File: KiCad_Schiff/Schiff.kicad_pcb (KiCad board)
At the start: 2 copper layers, 150 x 60 mm, 40 parts, among them J1 Conn_01x02, J2 L298N, J3 AMS1117-Module, J4 L298N, J5 Screw_Terminal_01x02, J6 Screw_Terminal_01x02, M1 Motor_Servo, M2 Motor_Servo, M3 Motor_Servo, SW1 SW_Wuerth_450301014042, SW2 SW_Wuerth_450301014042, U1 NRF24L01_Breakout

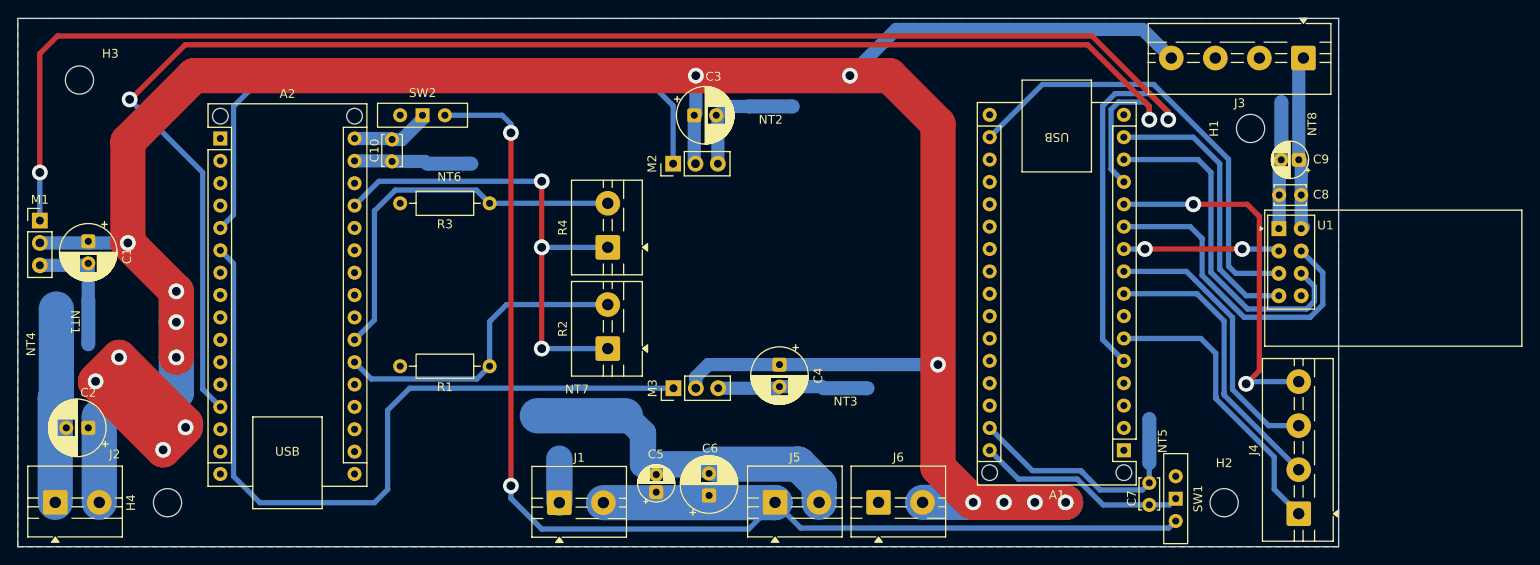
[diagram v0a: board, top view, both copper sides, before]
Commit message: Added plane on front
Added plane on front and put it on ground, to reduce machining
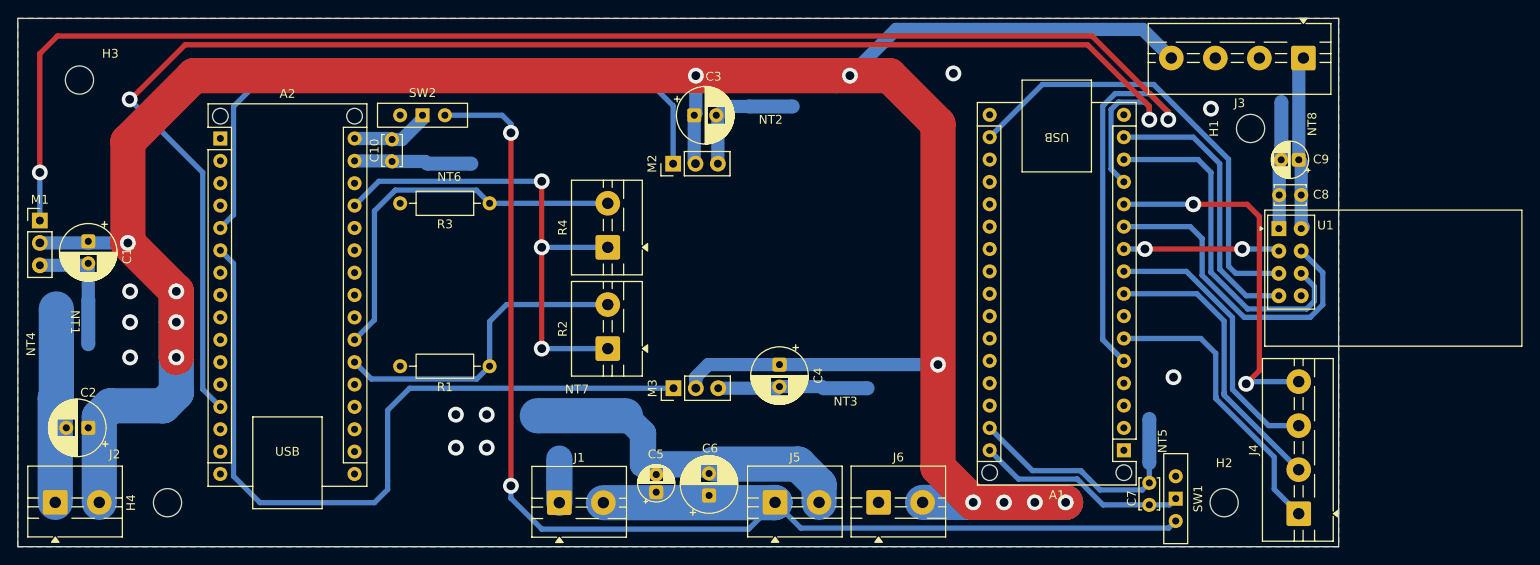
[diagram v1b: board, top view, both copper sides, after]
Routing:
- net /GND_PLANE: track 34.1 -> 5.00 mm, vias 4 -> 10
- added copper zone on F.Cu, net /GND_PLANE
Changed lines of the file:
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@@
 		(net 66)
 	)
-	(segment
-		(start 39 66)
-		(end 31.5 58.5)
-		(width 4)
-		(layer "F.Cu")
-		(net 67)
-	)
-	(segment
-		(start 39.05188 66.044315)
-		(end 39.007565 66)
-		(width 4)
-		(layer "F.Cu")
-		(net 67)
-	)
-	(segment
-		(start 39.007565 66)
-		(end 39 66)
-		(width 4)
-		(layer "F.Cu")
-		(net 67)
-	)
-	(segment
-		(start 28.827888 61.327888)
-		(end 28.827888 61.213147)
-		(width 4)
-		(layer "F.Cu")
-		(net 67)
-	)
-	(segment
-		(start 29 61.041035)
-		(end 29 61)
-		(width 4)
-		(layer "F.Cu")
-		(net 67)
-	)
-	(segment
-		(start 36.5 69)
-		(end 28.827888 61.327888)
-		(width 4)
-		(layer "F.Cu")
-		(net 67)
-	)
-	(segment
-		(start 39.05188 66.44812)
-		(end 36.5 69)
-		(width 4)
-		(layer "F.Cu")
-		(net 67)
-	)
-	(segment
-		(start 28.827888 61.213147)
-		(end 29 61.041035)
-		(width 4)
-		(layer "F.Cu")
-		(net 67)
-	)
-	(segment
-		(start 29 61)
-		(end 31.5 58.5)
-		(width 4)
-		(layer "F.Cu")
-		(net 67)
-	)
-	(via
-		(at 36.5 69)
-		(size 1.8)
-		(drill 1)
-		(layers "F.Cu" "B.Cu")
-		(free yes)
-		(net 67)
-	)
-	(via
-		(at 39.05188 66.44812)
-		(size 1.8)
-		(drill 1)
-		(layers "F.Cu" "B.Cu")
-		(free yes)
-		(net 67)
-	)
-	(via
-		(at 31.5 58.5)
-		(size 1.8)
-		(drill 1)
-		(layers "F.Cu" "B.Cu")
-		(free yes)
-		(net 67)
-	)
-	(via
-		(at 28.827888 61.213147)
+	(via
+		(at 73.25 68.75)
+		(size 1.8)
+		(drill 1)
+		(layers "F.Cu" "B.Cu")
+		(free yes)
+		(net 67)
+	)
+	(via
+		(at 69.75 65)
+		(size 1.8)
+		(drill 1)
+		(layers "F.Cu" "B.Cu")
+		(free yes)
+		(net 67)
+	)
+	(via
+		(at 32.75 51)
+		(size 1.8)
+		(drill 1)
+		(layers "F.Cu" "B.Cu")
+		(free yes)
+		(net 67)
+	)
+	(via
+		(at 151.25 60.75)
+		(size 1.8)
+		(drill 1)
+		(layers "F.Cu" "B.Cu")
+		(free yes)
+		(net 67)
+	)
+	(via
+		(at 155.5 30.25)
+		(size 1.8)
+		(drill 1)
+		(layers "F.Cu" "B.Cu")
+		(free yes)
+		(net 67)
+	)
+	(via
+		(at 32.75 58.5)
+		(size 1.8)
+		(drill 1)
+		(layers "F.Cu" "B.Cu")
+		(free yes)
+		(net 67)
+	)
+	(via
+		(at 69.75 68.75)
+		(size 1.8)
+		(drill 1)
+		(layers "F.Cu" "B.Cu")
+		(free yes)
+		(net 67)
+	)
+	(via
+		(at 73.25 65)
+		(size 1.8)
+		(drill 1)
+		(layers "F.Cu" "B.Cu")
+		(free yes)
+		(net 67)
+	)
+	(via
+		(at 32.75 54.5)
+		(size 1.8)
+		(drill 1)
+		(layers "F.Cu" "B.Cu")
+		(free yes)
+		(net 67)
+	)
+	(via
+		(at 126.25 26.25)
 		(size 1.8)
 		(drill 1)
@@
 		(net 67)
 		(net_name "/GND_PLANE")
-		(layer "B.Cu")
+		(layers "F.Cu" "B.Cu")
 		(name "Ground_Plane")
 		(hatch edge 0.5)

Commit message: Changed tracewidth
New tracewidth for voltage, because of thinner copper layer
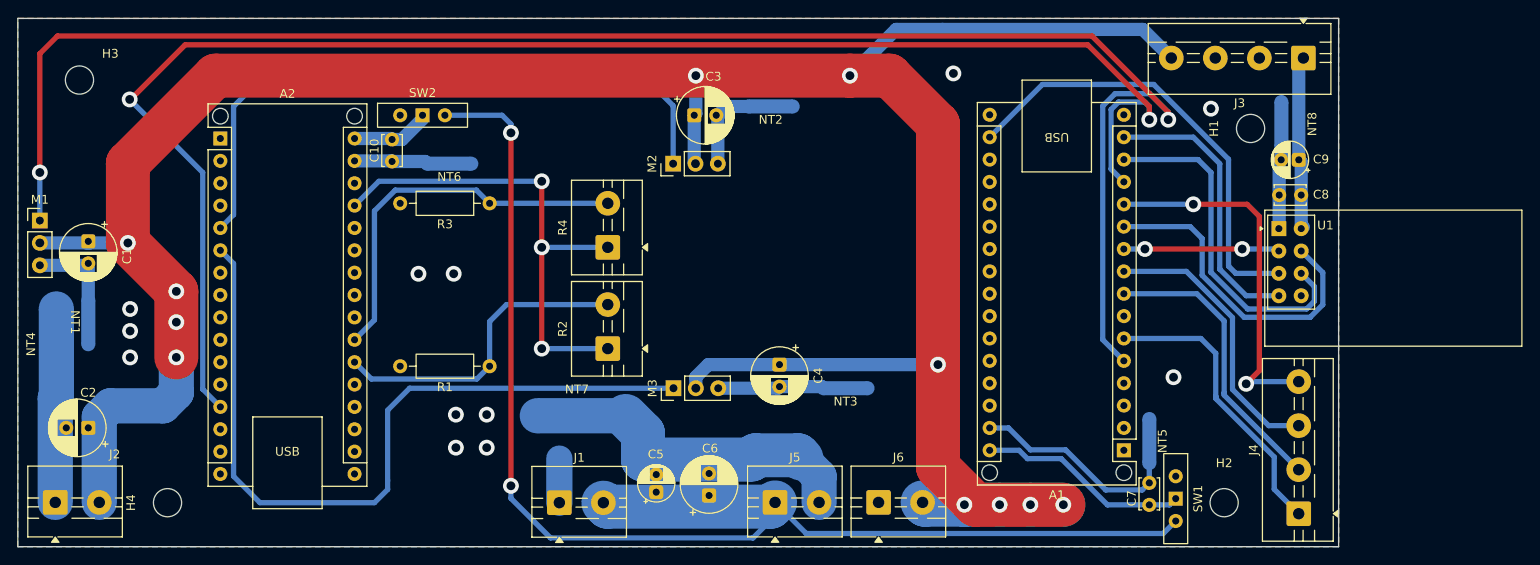
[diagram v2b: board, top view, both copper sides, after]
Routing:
- net VCC_BT: track 149.7 -> 152.3 mm
- net +5V: track 316.3 -> 314.6 mm
- net /GND_XL4015: track 29.3 -> 29.9 mm
- net /GND_PLANE: vias 10 -> 12
